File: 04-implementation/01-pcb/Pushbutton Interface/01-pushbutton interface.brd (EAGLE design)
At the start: 100 x 80 mm, 1 part

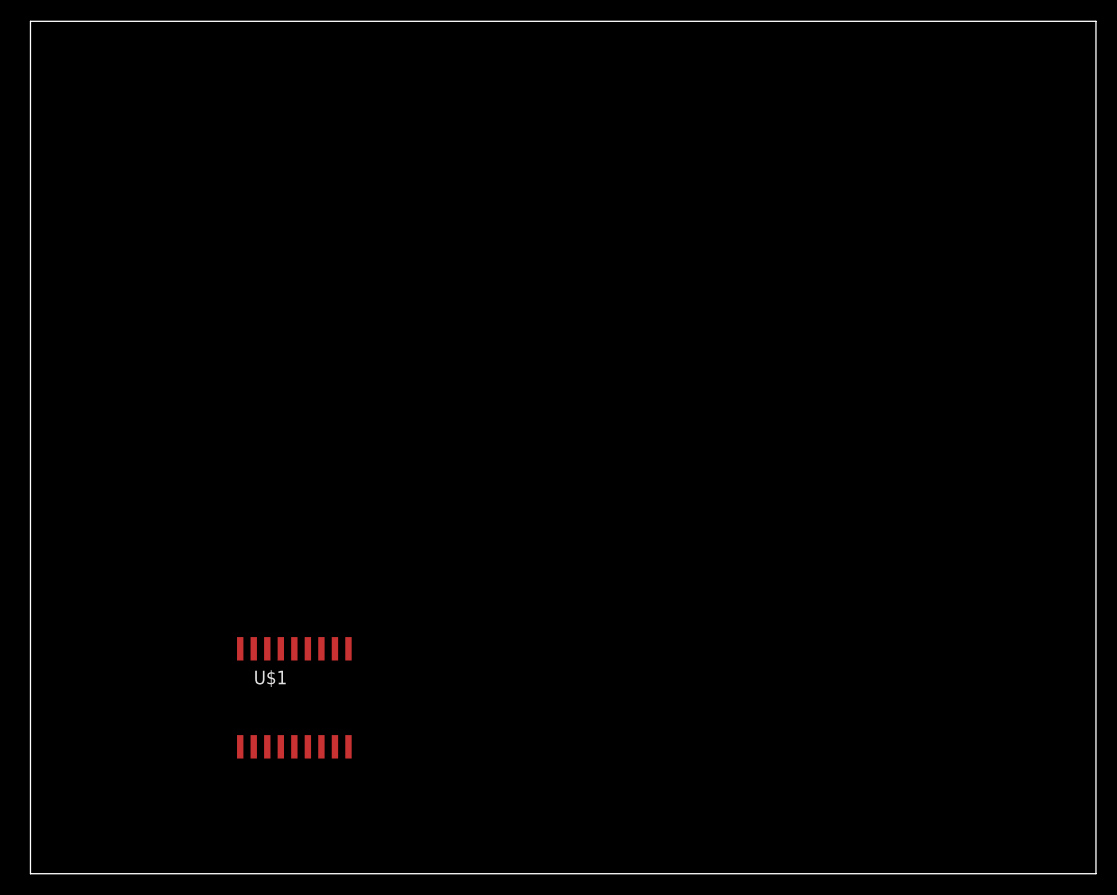
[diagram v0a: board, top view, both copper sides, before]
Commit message: Add files for initial placement of pushbutton interface.
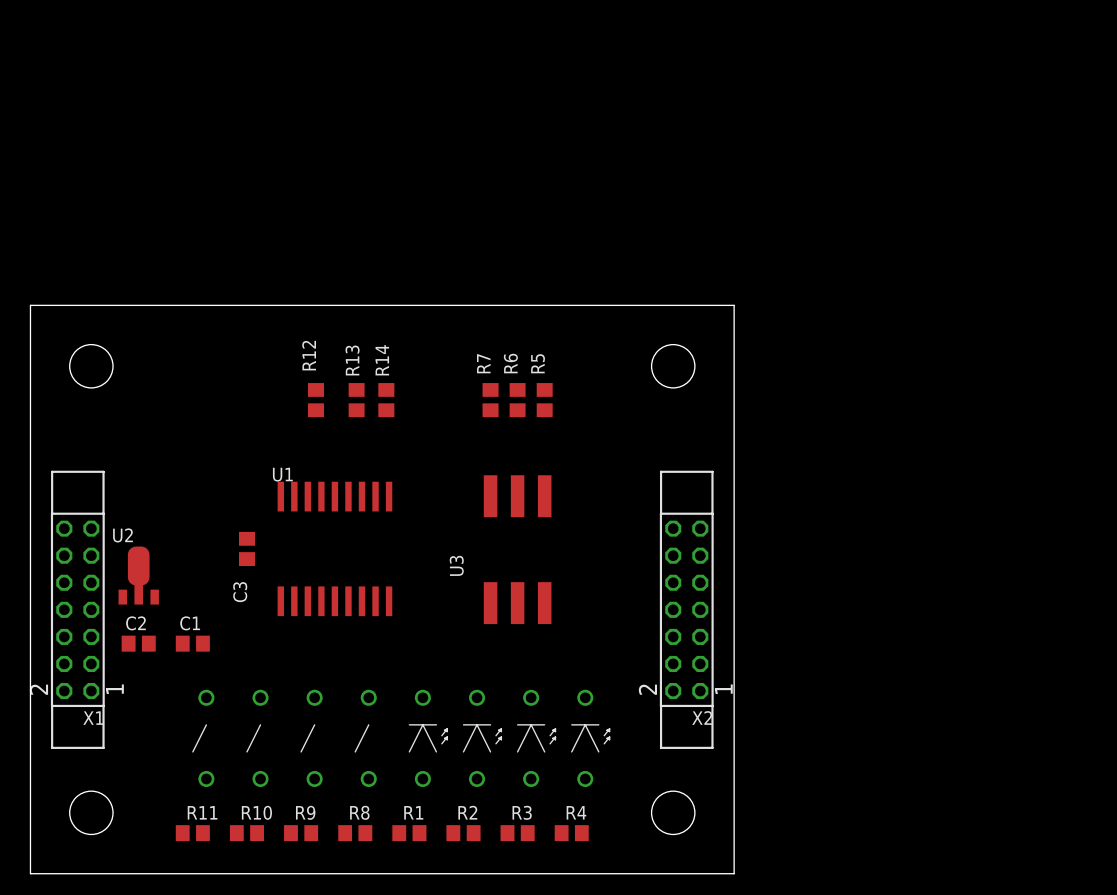
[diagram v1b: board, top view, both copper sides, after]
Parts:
- removed U$1: MCP23008, MIDI Pushbutton Parts:MCP23008-SO18
- added C1, C2: 1u, rcl:C0805
- added C3: 100n, rcl:C0805
- added LED1, LED2, LED3, LED4: 559-XXX-007, MIDI router parts:LED
- added R1, R2, R3, R4: 100, rcl:R0805
- added R10, R11, R12, R5, R6, R7, R8, R9: 100K, rcl:R0805
- added R13, R14: 2.2K, rcl:R0805
- added SW1, SW2, SW3, SW4: PB-SWITCH, MIDI router parts:SWITCH
- added U1: MCP23008, MIDI router parts:MCP23008-SO18
- added U2: MCP1700-SOT89, MIDI router parts:MCP1700-SOT89
- added U3: 219-3LPSTR, MIDI router parts:219-3LPSTR
- added X1, X2: SSW-107-02-G-D, MIDI router parts:SSW-107-02-G-D
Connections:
- new net +3V3: C1.1, C3.1, R1.1, R10.1, R11.1, R12.1, R13.1, R14.1, R2.1, R3.1, R4.1, R5.1, R6.1, R7.1, R8.1, R9.1, U1.18, U2.3
- new net +5V: C2.1, U2.2, U2.2@1, X1.1, X1.14, X2.1, X2.14
- new net GND: C1.2, C2.2, C3.2, SW1.P$2, SW2.P$2, SW3.P$2, SW4.P$2, U1.9, U2.1, U3.1, U3.2, U3.3, X1.13, X1.2, X2.13, X2.2
- new net N$1: R8.2, SW1.P$1, U1.13
- new net N$10: LED4.P$2, U1.14
- new net N$11: R7.2, U1.3, U3.6
- new net N$12: R6.2, U1.4, U3.5
- new net N$13: R5.2, U1.5, U3.4
- new net N$14: R10.2, SW3.P$1, U1.11
- new net N$15: R11.2, SW4.P$1, U1.10
- new net N$16: R12.2, U1.6
- new net N$2: R9.2, SW2.P$1, U1.12
- new net N$3: LED4.P$1, R1.2
- new net N$4: LED3.P$1, R2.2
- new net N$5: LED2.P$1, R3.2
- new net N$6: LED1.P$1, R4.2
- new net N$7: LED1.P$2, U1.17
- new net N$8: LED2.P$2, U1.16
- new net N$9: LED3.P$2, U1.15
- new net SCL: R14.2, U1.1, X1.11, X1.12, X2.11, X2.12
- new net SDA: R13.2, U1.2, X1.10, X1.9, X2.10, X2.9
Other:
- board size 100 x 80 mm -> 66 x 53.3 mm

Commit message: Add files for pushbutton PCB.
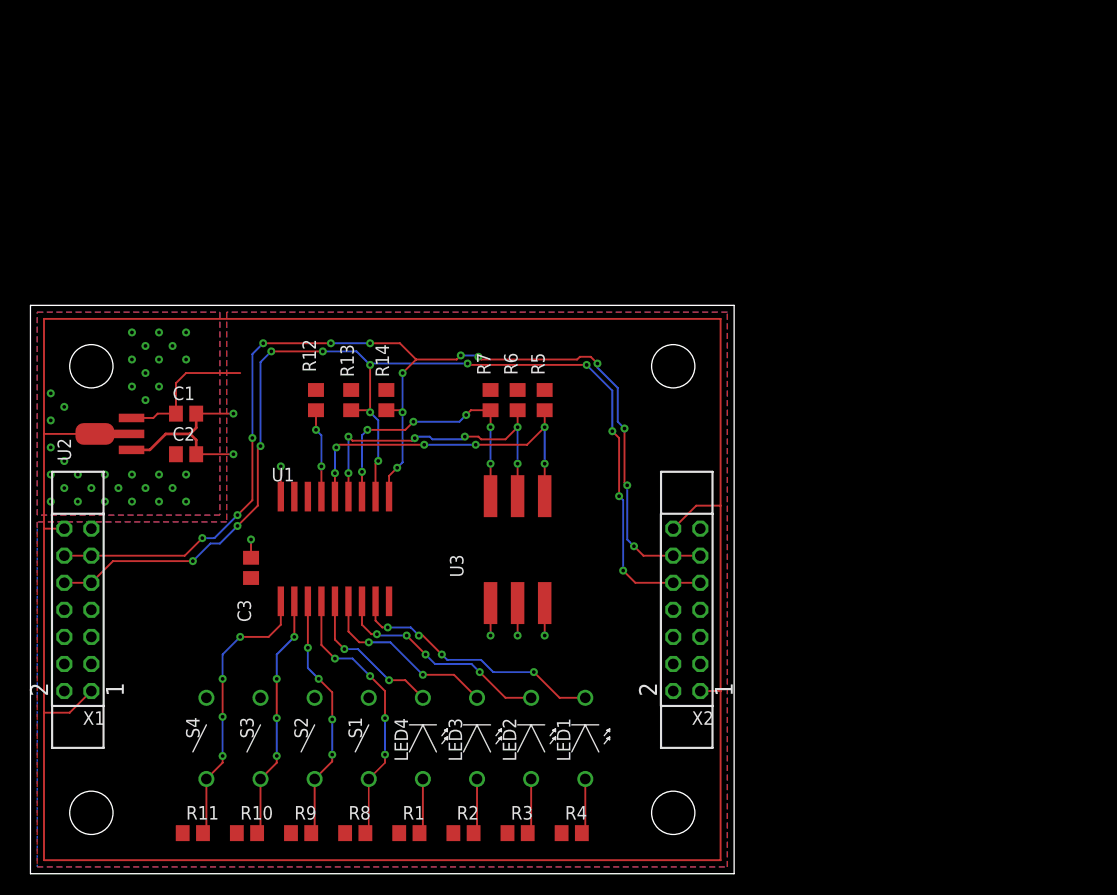
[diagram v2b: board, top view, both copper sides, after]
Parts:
- moved C1 21.6 mm to (14.6, 43.2)
- moved C2 18.3 mm to (14.6, 39.4)
- moved U2 13.7 mm to (6.99, 41.3), turned to 90 degrees
- moved C3 1.82 mm to (20.7, 28.7)
- moved R13 0.51 mm to (30.1, 44.5)
- renumbered SW1 to S1, SW2 to S2, SW3 to S3, SW4 to S4
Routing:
- net +5V: track 0.00 -> 247.8 mm, vias 0 -> 34
- net SDA: track 0.00 -> 109.5 mm, vias 0 -> 13
- net SCL: track 0.00 -> 108.3 mm, vias 0 -> 15
- net N$13: track 0.00 -> 33.1 mm, vias 0 -> 6
- net GND: track 0.00 -> 31.1 mm, vias 0 -> 7
- net N$12: track 0.00 -> 30.7 mm, vias 0 -> 6
- net N$11: track 0.00 -> 26.9 mm, vias 0 -> 6
- net N$15: track 0.00 -> 26.3 mm, vias 0 -> 4
- net N$1: track 0.00 -> 26.0 mm, vias 0 -> 4
- net N$7: track 0.00 -> 24.5 mm, vias 0 -> 4
- net N$2: track 0.00 -> 23.5 mm, vias 0 -> 4
- net N$14: track 0.00 -> 23.2 mm, vias 0 -> 4
- net N$8: track 0.00 -> 20.9 mm, vias 0 -> 4
- net N$9: track 0.00 -> 17.5 mm, vias 0 -> 2
- net N$10: track 0.00 -> 14.1 mm, vias 0 -> 2
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- added copper zone on layer 1, net +3V3
- added copper zone on layer 1, net +5V
- added copper zone on layer 16, net +5V
- added copper zone on layer 16, net GND
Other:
- board text added: "HW0005"
- board text added: "R001"
